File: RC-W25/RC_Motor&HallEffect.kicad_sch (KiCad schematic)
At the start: 10 parts, among them Q1 NMOS, SW1 SW_MEC_5G, SW2 SW_MEC_5G

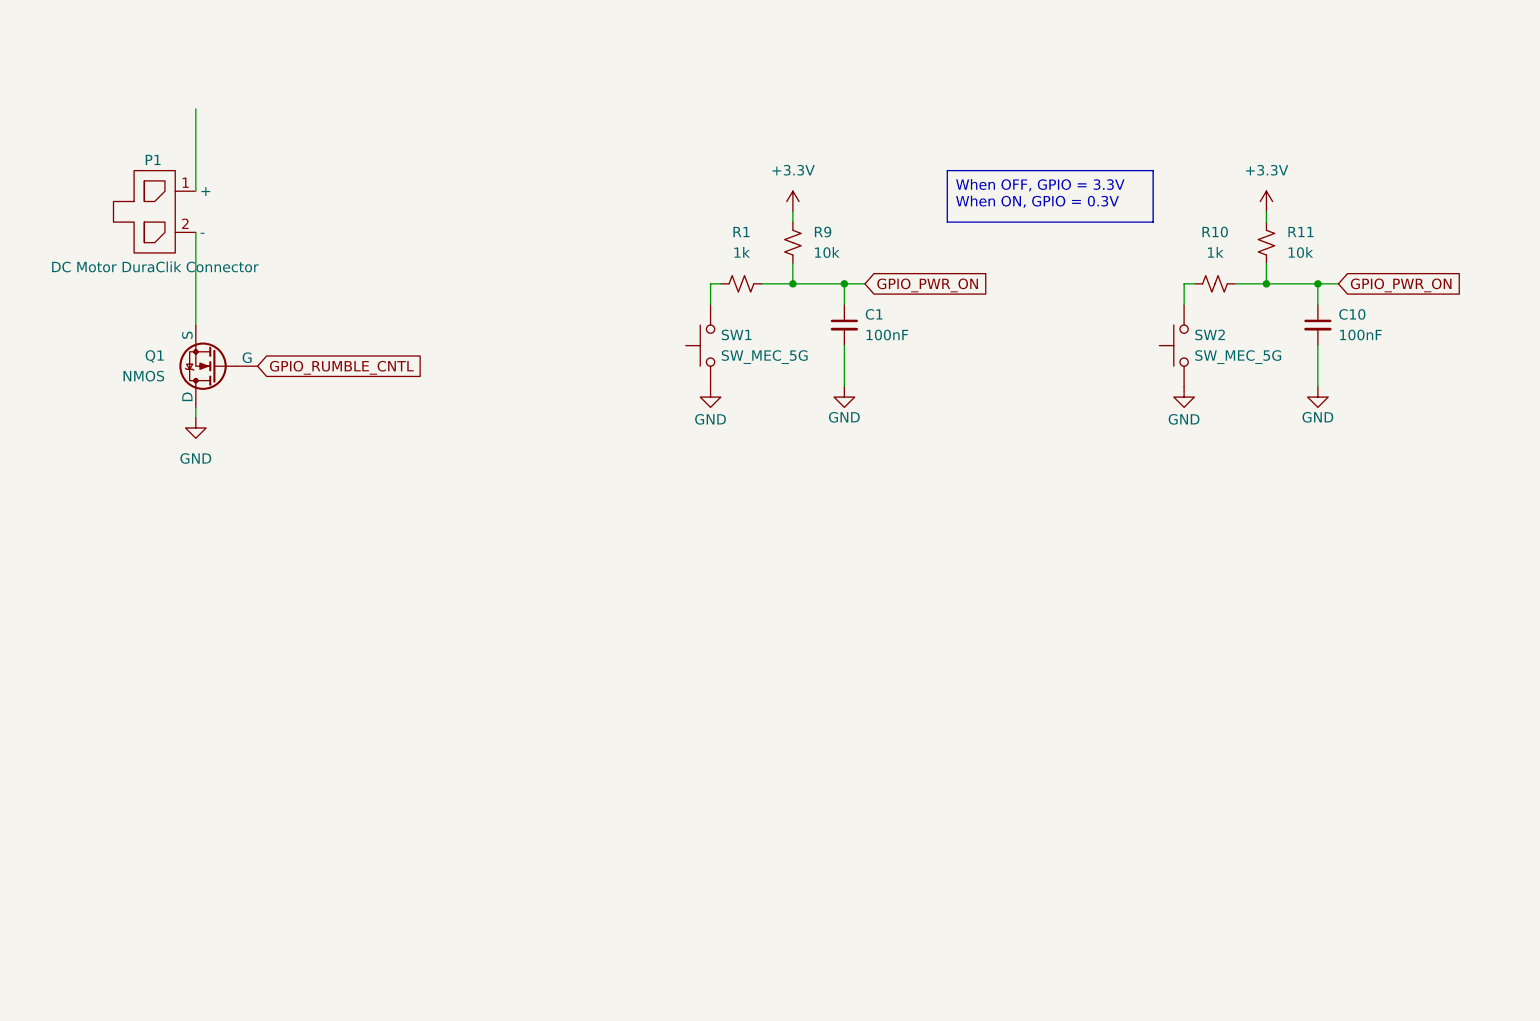
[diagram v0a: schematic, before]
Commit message: Updated Schematic
Introduced linear hall effect sensors
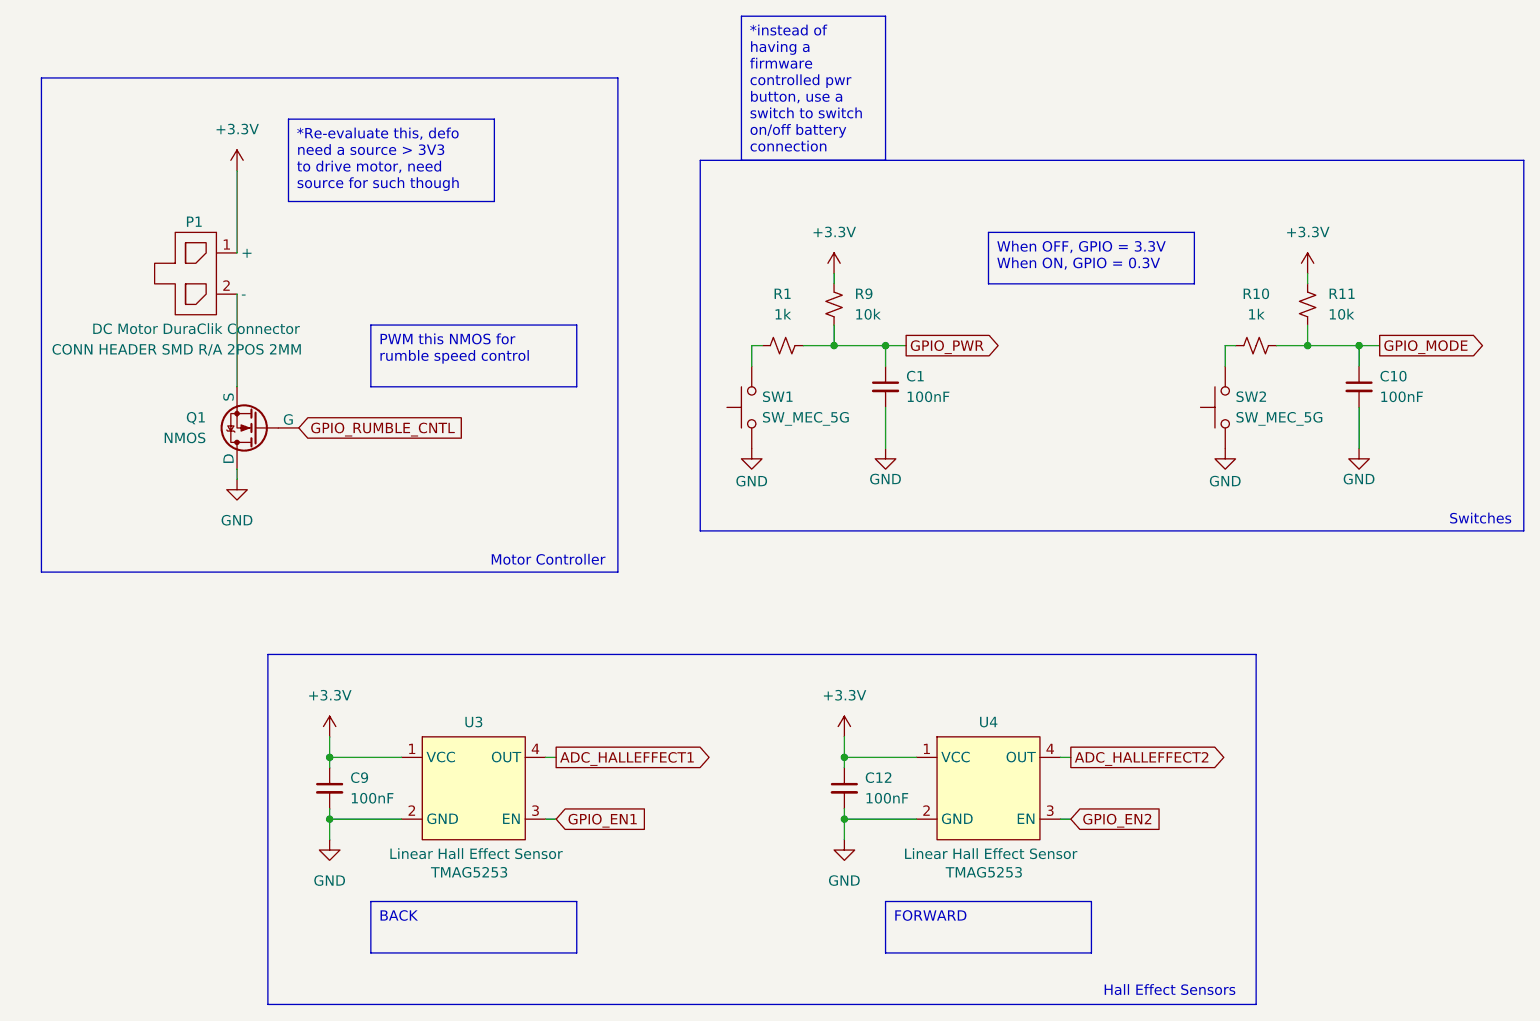
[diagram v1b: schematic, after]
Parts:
- added C12, C9: 100nF, Capacitor_SMD:C_0603_1608Metric, symbol Device:C_Small
- added U3, U4: TMAG5253, symbol New_Library_0:TMAG5253_Linear_Hall_Effect_Sensor
- P1: value ~ -> CONN HEADER SMD R/A 2POS 2MM
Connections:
- net +3.3V: now also C12.1, C9.1, U3.1 (VCC), U4.1 (VCC)
- net GND: now also C12.2, C9.2, U3.2 (GND), U4.2 (GND)
- net GPIO_PWR_ON renamed GPIO_MODE
- net GPIO_MODE: no longer C1.1, R1.2, R9.1
- new net ADC_HALLEFFECT1: U3.4 (OUT)
- new net ADC_HALLEFFECT2: U4.4 (OUT)
- new net GPIO_EN1: U3.3 (EN)
- new net GPIO_EN2: U4.3 (EN)
- new net GPIO_PWR: C1.1, R1.2, R9.1
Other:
- note added: "Hall Effect Sensors"
- note added: "Motor Controller"
- note added: "Switches"
- moved on the sheet: C1, C10, P1, Q1, R1, R10, R11, R9, SW1, SW2

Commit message: Updated Battery
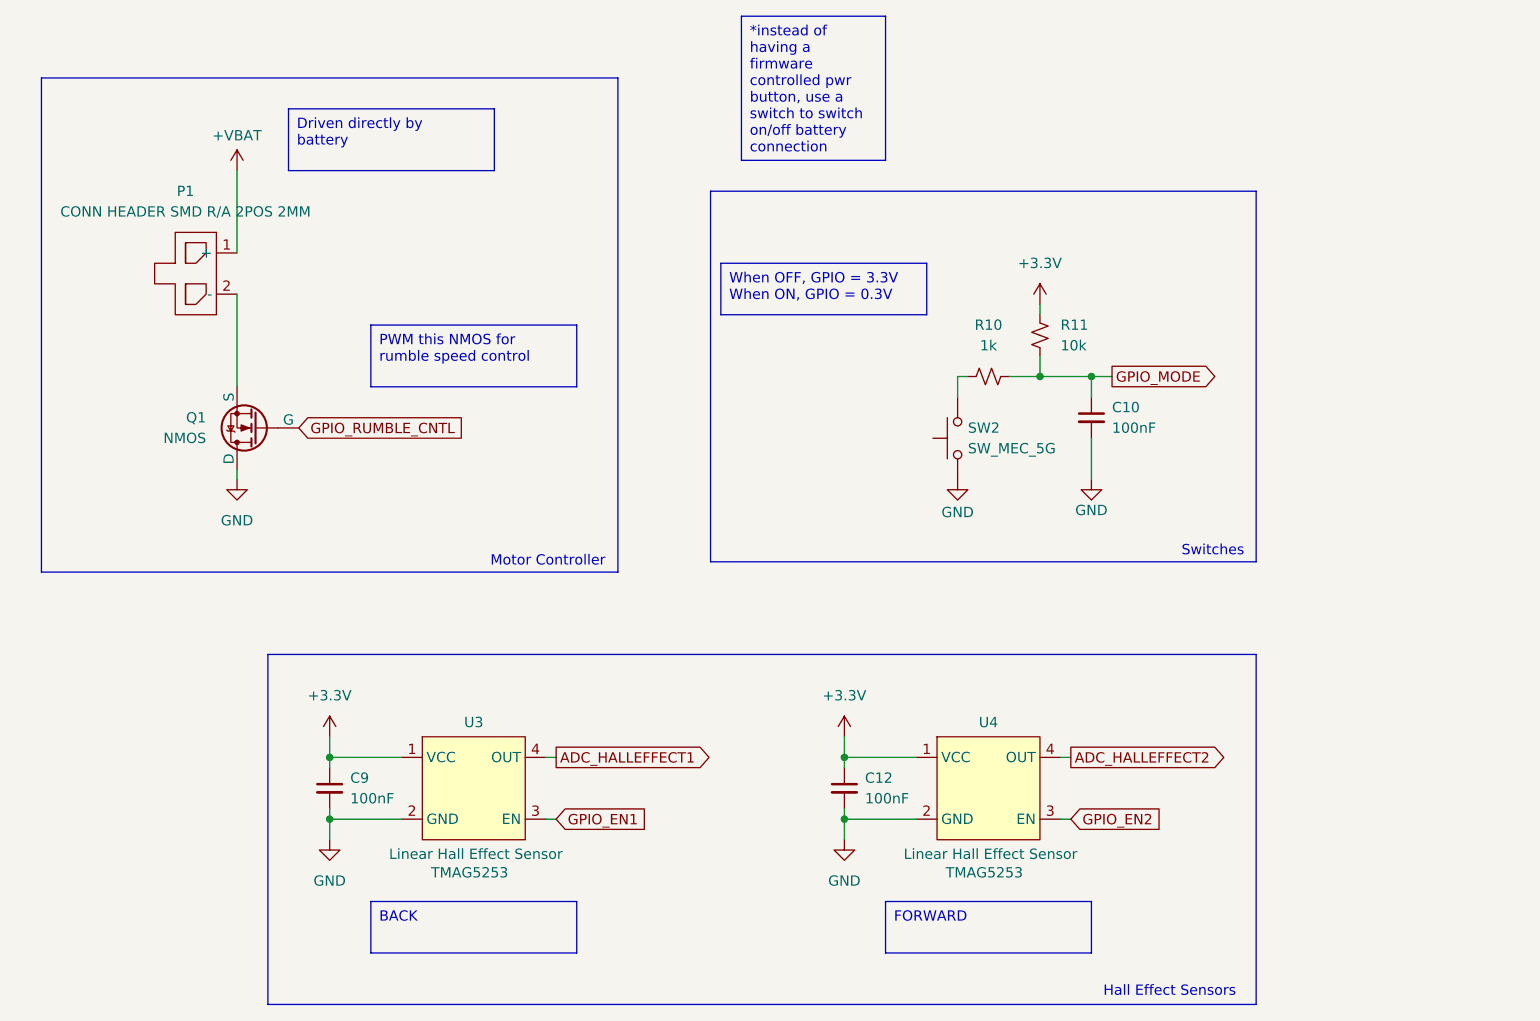
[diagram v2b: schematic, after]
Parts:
- removed C1: 100nF, Capacitor_SMD:C_0603_1608Metric, symbol Device:C_Small
- removed R1: 1k, Resistor_SMD:R_0603_1608Metric, symbol Device:R_Small_US
- removed R9: 10k, Resistor_SMD:R_0603_1608Metric, symbol Device:R_Small_US
- removed SW1: SW_MEC_5G, symbol Switch:SW_MEC_5G
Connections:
- net +VBAT: now reaches P1.1 (+)
- net at P1.2 (-): now also Q1.3 (S)
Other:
- moved on the sheet: C10, R10, R11, SW2

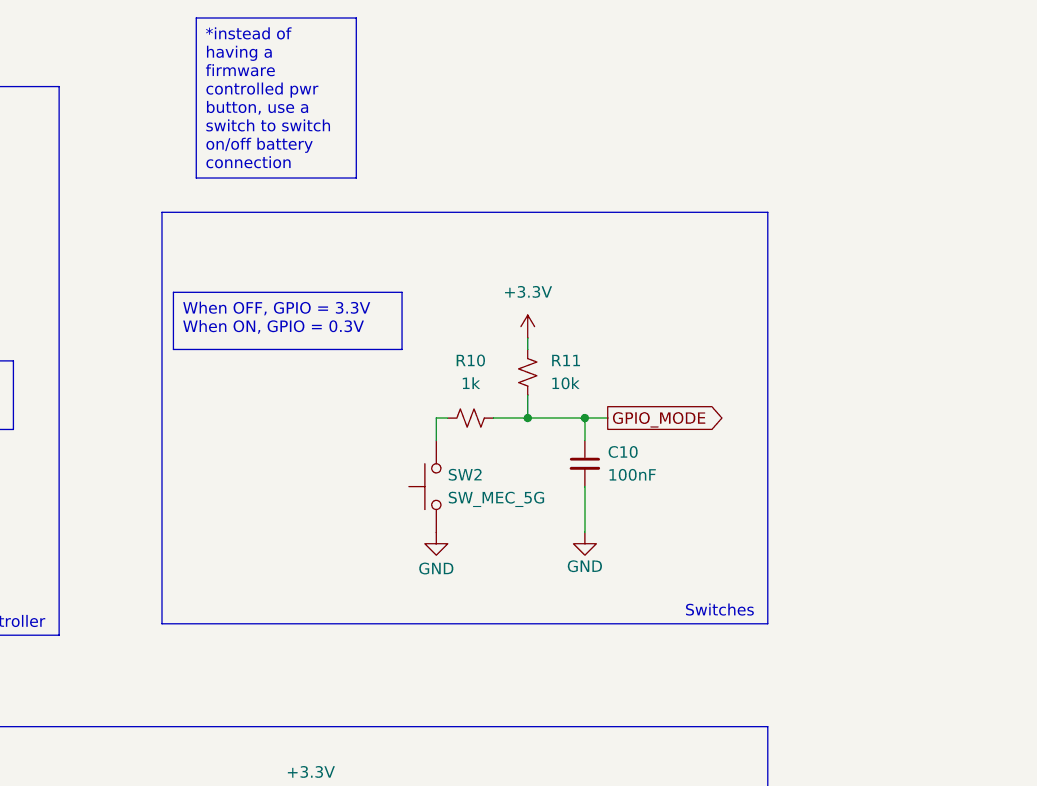
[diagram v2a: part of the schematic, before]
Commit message: Updated Footprints
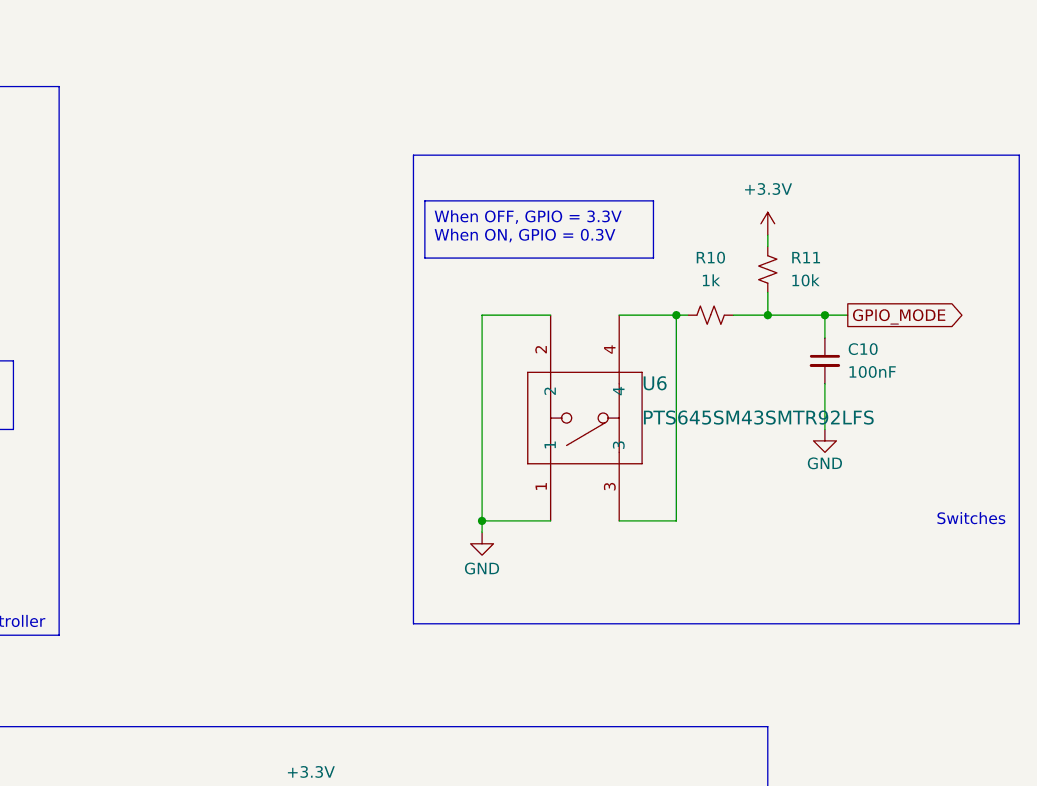
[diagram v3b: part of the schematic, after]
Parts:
- removed SW2: SW_MEC_5G, symbol Switch:SW_MEC_5G
- added U6: PTS645SM43SMTR92LFS, Library:SWITCH_43SMTR92LFS, symbol New_Library_5:PTS645SM43SMTR92LFS
- P1: footprint (none) -> Library:CONN02_502352_MOL
- Q1: footprint (none) -> Sensor:SOT-23_2P9X1P3_DIO
- U3, U4: footprint (none) -> Library:X2SON4_DMR_TEX-M
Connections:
- net GND: now also U6.1, U6.2
- net at R10.1: now also U6.3, U6.4
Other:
- moved on the sheet: C10, R10, R11

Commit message: Almost Finalized Schematic
Still need to spec out buttons and jst conn
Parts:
- removed C10, C12: 100nF, Capacitor_SMD:C_0603_1608Metric, symbol Device:C_Small
- removed P1: CONN HEADER SMD R/A 2POS 2MM, Library:CONN02_502352_MOL, symbol New_Library:DuraClik_CONN_HEADER_SMD_R/A_2POS_2MM
- removed R10: 1k, Resistor_SMD:R_0603_1608Metric, symbol Device:R_Small_US
- removed R11: 10k, Resistor_SMD:R_0603_1608Metric, symbol Device:R_Small_US
- removed U4: TMAG5253, Library:X2SON4_DMR_TEX-M, symbol New_Library_0:TMAG5253_Linear_Hall_Effect_Sensor
- removed U6: PTS645SM43SMTR92LFS, Library:SWITCH_43SMTR92LFS, symbol New_Library_5:PTS645SM43SMTR92LFS
- added C17, C18: 100nF, Capacitor_SMD:C_0402_1005Metric, symbol Device:C_Small
- added D5: D_Schottky, Diode_SMD:D_SOD-123, symbol Device:D_Schottky
- added P2: JST CONN, Library:CONN02_502352_MOL, symbol Connector_Generic:Conn_01x02
- added R14, R15: 10k, Resistor_SMD:R_0402_1005Metric, symbol Device:R_Small_US
- added SW2: Button, symbol Switch:SW_Push
- added U5: TMAG5253, Library:X2SON4_DMR_TEX-M, symbol New_Library_0:TMAG5253_Linear_Hall_Effect_Sensor
- C16: renamed from C9; footprint Capacitor_SMD:C_0603_1608Metric -> Capacitor_SMD:C_0402_1005Metric; LCSC# (none) -> C22435938
- U4: renamed from U3; LCSC# (none) -> C22445458
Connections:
- net +3.3V: now also C17.1, R14.1, U5.1 (VCC)
- net +VBAT: now also D5.1 (K), P2.1 (Pin_1)
- net ADC_HALLEFFECT2: now also U5.4 (OUT)
- net GND: now also C17.2, C18.2, SW2.2, U5.2 (GND)
- net GPIO_EN2: now also U5.3 (EN)
- net GPIO_MODE: now also C18.1, R15.2
- net at Q1.3 (S): now also D5.2 (A), P2.2 (Pin_2)
- new net: R14.2, R15.1, SW2.1
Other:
- note added: "HFS"
- note added: "Mode Select"
- note removed: "Hall Effect Sensors"
- note removed: "Switches"
- moved on the sheet: C16, Q1, U4
